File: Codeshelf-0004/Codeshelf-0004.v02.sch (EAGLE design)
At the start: 13 parts, among them J5 HEADER-2X-2.54MM

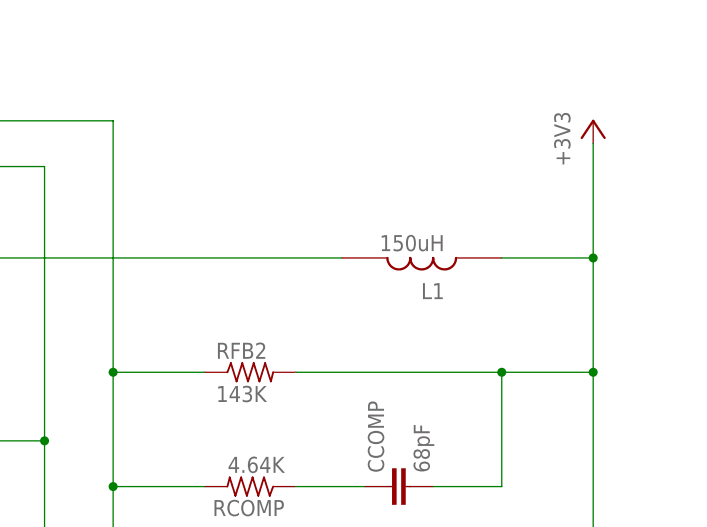
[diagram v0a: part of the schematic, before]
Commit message: SlotFlex Pos. Controller, SMPS
Copied position controller elements to Slotflex schematic. Corrected
inductor value typo in SMPS.
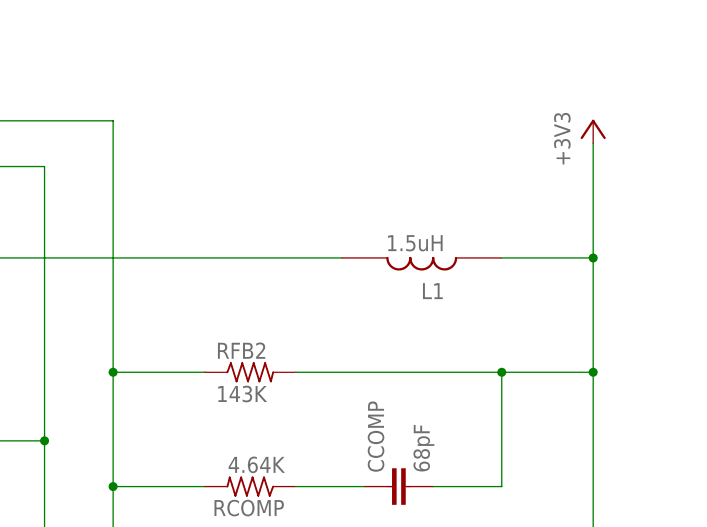
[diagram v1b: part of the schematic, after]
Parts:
- L1: value 150uH -> 1.5uH
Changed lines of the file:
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@@
 <attribute name="PRICE" value="0.03"/>
 </part>
-<part name="L1" library="GW-devices" deviceset="INDUCTOR-SMD-UNUSUAL" device="-SLF10165" value="150uH">
+<part name="L1" library="GW-devices" deviceset="INDUCTOR-SMD-UNUSUAL" device="-SLF10165" value="1.5uH">
 <attribute name="MFGN" value="TDK"/>
 <attribute name="MFGP" value="SLF10165T-1R5N6R83PF"/>

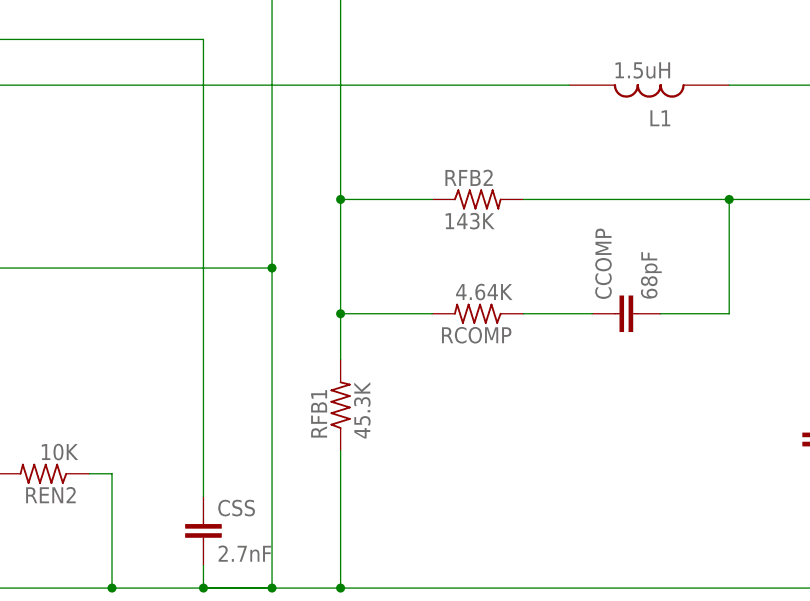
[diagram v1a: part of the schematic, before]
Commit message: Fixed FB resistor label
Made FB1/FB2 resistor label consistent with datasheet. but NOT with
online calculator
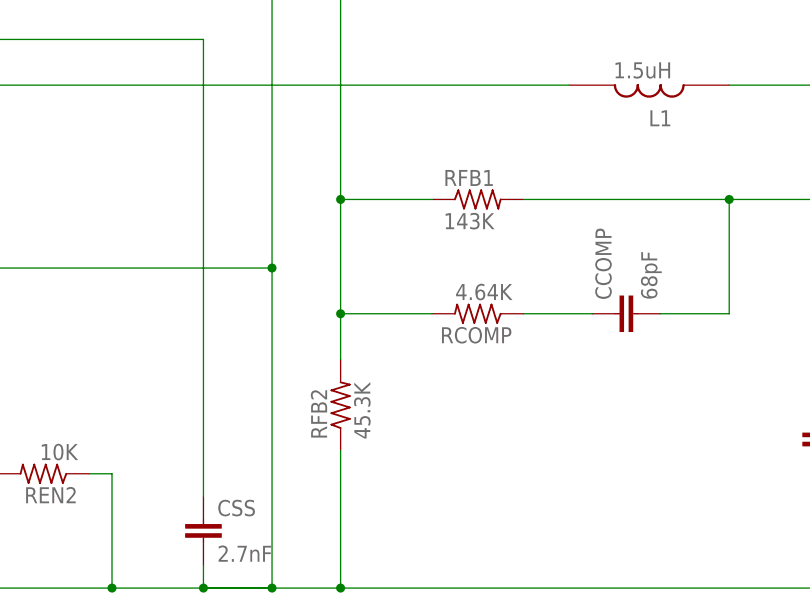
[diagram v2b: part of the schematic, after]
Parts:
- RFB1: value 45.3K -> 143K; MFGP CRCW040245K3FKED -> CRCW0402143KFKED; PRICE 0.04 -> 0.05
- RFB2: value 143K -> 45.3K; MFGP CRCW0402143KFKED -> CRCW040245K3FKED; PRICE 0.05 -> 0.04
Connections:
- net +3V3: now also RFB1.2; no longer RFB2.2
- net GND: now also RFB2.1; no longer RFB1.1
- net N$24: now also RFB1.1, RFB2.2; no longer RFB1.2, RFB2.1
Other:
- moved on the sheet: RFB1, RFB2
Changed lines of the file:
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@@
 <part name="GND9" library="supply1" deviceset="GND" device=""/>
 <part name="+3V9" library="supply1" deviceset="+3V3" device=""/>
-<part name="RFB2" library="GW-devices" deviceset="RF-R" device="0402" value="143K">
+<part name="RFB1" library="GW-devices" deviceset="RF-R" device="0402" value="143K">
 <attribute name="MFGN" value="Vishay"/>
 <attribute name="MFGP" value="CRCW0402143KFKED"/>
 <attribute name="PRICE" value="0.05"/>
 </part>
-<part name="RFB1" library="GW-devices" deviceset="RF-R" device="0402" value="45.3K">
+<part name="RFB2" library="GW-devices" deviceset="RF-R" device="0402" value="45.3K">
 <attribute name="MFGN" value="Vishay"/>
 <attribute name="MFGP" value="CRCW040245K3FKED"/>
@@
 <instance part="GND9" gate="1" x="546.1" y="-5.08"/>
 <instance part="+3V9" gate="G$1" x="546.1" y="76.2"/>
-<instance part="RFB2" gate="G$1" x="508" y="48.26">
+<instance part="RFB1" gate="G$1" x="508" y="48.26">
 <attribute name="MFGN" x="508" y="48.26" size="1.778" layer="96" display="off"/>
 <attribute name="MFGP" x="508" y="48.26" size="1.778" layer="96" display="off"/>
 <attribute name="PRICE" x="508" y="48.26" size="1.778" layer="96" display="off"/>
 </instance>
-<instance part="RFB1" gate="G$1" x="492.76" y="25.4" rot="R90">
+<instance part="RFB2" gate="G$1" x="492.76" y="25.4" rot="R90">
 <attribute name="MFGN" x="492.76" y="25.4" size="1.778" layer="96" rot="R90" display="off"/>
 <attribute name="MFGP" x="492.76" y="25.4" size="1.778" layer="96" rot="R90" display="off"/>
@@
 <pinref part="CSS" gate="G$1" pin="2"/>
 <pinref part="GND9" gate="1" pin="GND"/>
-<pinref part="RFB1" gate="G$1" pin="1"/>
+<pinref part="RFB2" gate="G$1" pin="1"/>
 <pinref part="COUT1" gate="G$1" pin="2"/>
 <pinref part="REN2" gate="G$1" pin="1"/>
@@
 <pinref part="L1" gate="1" pin="2"/>
 <pinref part="+3V9" gate="G$1" pin="+3V3"/>
-<pinref part="RFB2" gate="G$1" pin="2"/>
+<pinref part="RFB1" gate="G$1" pin="2"/>
 <pinref part="CCOMP" gate="G$1" pin="2"/>
 <pinref part="COUT1" gate="G$1" pin="1"/>
@@
 <junction x="492.76" y="35.56"/>
 <pinref part="U-P1" gate="G$1" pin="FB"/>
-<pinref part="RFB2" gate="G$1" pin="1"/>
-<pinref part="RFB1" gate="G$1" pin="2"/>
+<pinref part="RFB1" gate="G$1" pin="1"/>
+<pinref part="RFB2" gate="G$1" pin="2"/>
 <pinref part="RCOMP" gate="G$1" pin="2"/>
 </segment>
